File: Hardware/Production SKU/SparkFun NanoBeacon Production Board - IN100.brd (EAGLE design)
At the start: 25.4 x 25.4 mm, 63 parts, among them J3 Vertical Qwiic Connector, U1 IN100, Y1 CRYSTAL-26MHZSMD-3.2X2.5

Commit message: v11 updates
Bump version number
Update board name in silk
Change "VBATT" silk to "Battery"
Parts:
- removed U$10: (no value), output:BEACON_#_IN1000
- removed U$27: (no value), output:VBATT_OR_VCC_ONLY##0
- added U$29: (no value), output:NANOBEACON0
- added U$31: (no value), output:IN1000
- U$1: device output:BLUETOOTH0 -> output:NANOBEACON0
- U$5: device output:BEACON_#_IN1000 -> output:IN1000
- U$9: device output:BLUETOOTH0 -> output:BATTERY_OR_VCC_ONLY##0
- moved U$9 18.4 mm to (12.7, 0.89), flipped to the top
- moved U$5 2.92 mm to (12.7, 17.5), flipped to the bottom
- moved U$1 2.67 mm to (12.7, 19.2), flipped to the bottom
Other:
- board text added: "v11"
- board text removed: "v10"
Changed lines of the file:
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@@
 <drawing>
 <settings>
-<setting alwaysvectorfont="no"/>
+<setting alwaysvectorfont="yes"/>
 <setting verticaltext="up"/>
 </settings>
@@
 <vertex x="21.865" y="18.33"/>
 </polygon>
-<text x="12.7" y="0.889" size="1.27" layer="16" font="vector" ratio="15" rot="MR0" align="center">v10</text>
+<text x="12.7" y="0.889" size="1.27" layer="16" font="vector" ratio="15" rot="MR0" align="center">v11</text>
 <polygon width="0.1016" layer="22">
 <vertex x="19.05" y="8.89"/>
@@
 <attribute name="VALUE" x="16.48366875" y="15.224" size="0.6096" layer="27" rot="R270"/>
 </element>
-<element name="U$1" library="output" package="BLUETOOTH0" value="" x="12.7" y="21.844" smashed="yes"/>
 <element name="U$4" library="SparkFun-Aesthetics" package="SFE_LOGO_NAME_.1" value="" x="12.7" y="23.749" smashed="yes"/>
-<element name="U$5" library="output" package="BEACON_#_IN1000" value="" x="12.7" y="20.447" smashed="yes"/>
 <element name="U$2" library="output" package="#_7#0" value="" x="1.397" y="19.05" smashed="yes"/>
 <element name="U$3" library="output" package="#_6#0" value="" x="1.397" y="16.51" smashed="yes"/>
@@
 <element name="LOGO1" library="SparkFun-Aesthetics" package="OSHW-LOGO-S" value="OSHW-LOGOS" x="12.7" y="11.43" smashed="yes" rot="MR0"/>
 <element name="LOGO2" library="SparkFun-Aesthetics" package="SFE_LOGO_NAME_FLAME_.1" value="SFE_LOGO_NAME_FLAME.1_INCH" x="12.7" y="21.59" smashed="yes" rot="MR0"/>
-<element name="U$9" library="output" package="BLUETOOTH0" value="" x="12.7" y="19.304" smashed="yes" rot="MR0"/>
-<element name="U$10" library="output" package="BEACON_#_IN1000" value="" x="12.7" y="17.907" smashed="yes" rot="MR0"/>
 <element name="U$13" library="output" package="#IO7_#0" value="" x="1.27" y="19.05" smashed="yes" rot="MR0"/>
 <element name="U$14" library="output" package="#IO6_#0" value="" x="1.27" y="16.51" smashed="yes" rot="MR0"/>
@@
 <element name="U$26" library="output" package="PWR0" value="" x="5.08" y="9.271" smashed="yes"/>
 <element name="U$12" library="output" package="#NOTES#0" value="" x="16.129" y="8.89" smashed="yes" rot="MR0"/>
-<element name="U$27" library="output" package="VBATT_OR_VCC_ONLY##0" value="" x="12.7" y="0.889" smashed="yes"/>
 <element name="RST" library="SparkFun-Switches" package="TACTILE_SWITCH_SMD_4.6X2.8MM" value="DNP" x="6.35" y="14.732" smashed="yes">
 <attribute name="NAME" x="6.35" y="16.256" size="0.6096" layer="25" font="vector" ratio="20" align="bottom-center"/>
@@
 <element name="U$30" library="output" package="PRO0" value="" x="21.59" y="24.003" smashed="yes"/>
 <element name="TP3" library="SparkFun-Connectors" package="PAD.03X.03" value="TEST-POINT3" x="6.35" y="15.875" smashed="yes" rot="MR0"/>
+<element name="U$29" library="output" package="NANOBEACON0" value="" x="12.7" y="21.844" smashed="yes"/>
+<element name="U$31" library="output" package="IN1000" value="" x="12.7" y="20.32" smashed="yes"/>
+<element name="U$1" library="output" package="NANOBEACON0" value="" x="12.7" y="19.177" smashed="yes" rot="MR0"/>
+<element name="U$5" library="output" package="IN1000" value="" x="12.7" y="17.526" smashed="yes" rot="MR0"/>
+<element name="U$9" library="output" package="BATTERY_OR_VCC_ONLY##0" value="" x="12.7" y="0.889" smashed="yes"/>
 </elements>
 <signals>

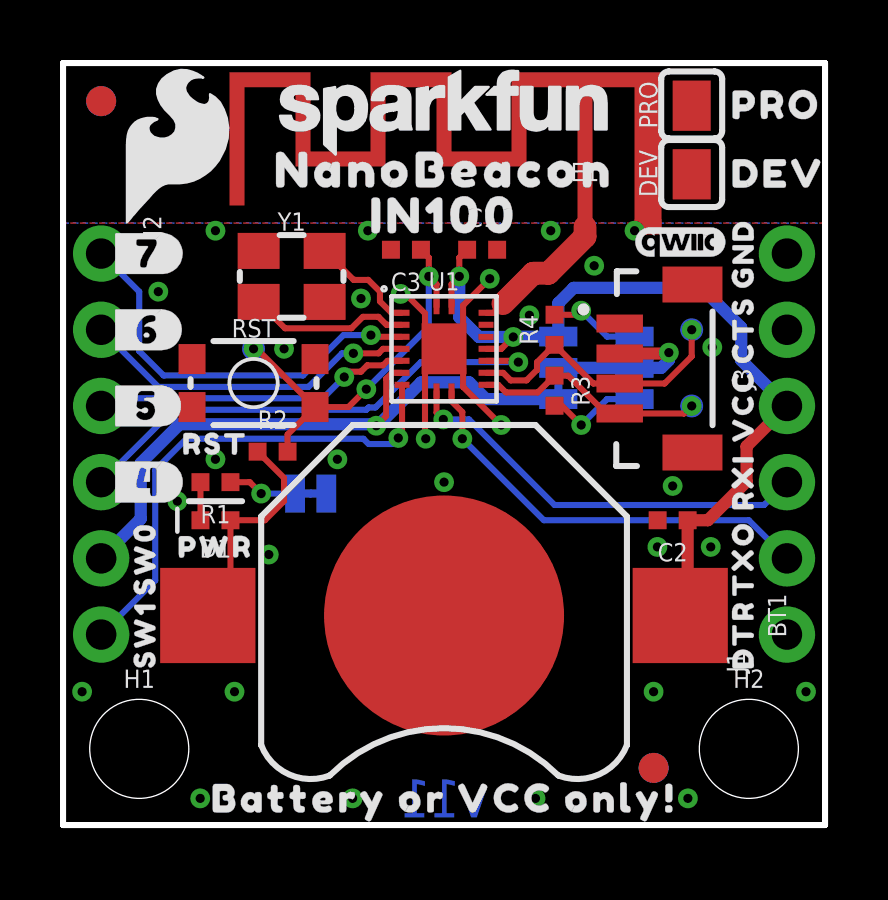
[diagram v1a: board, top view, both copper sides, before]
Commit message: Minor updates
Nudge bottom SFE silk logo away from edge
Increase size of Qwiic logo
Nudge vias along bottom edge
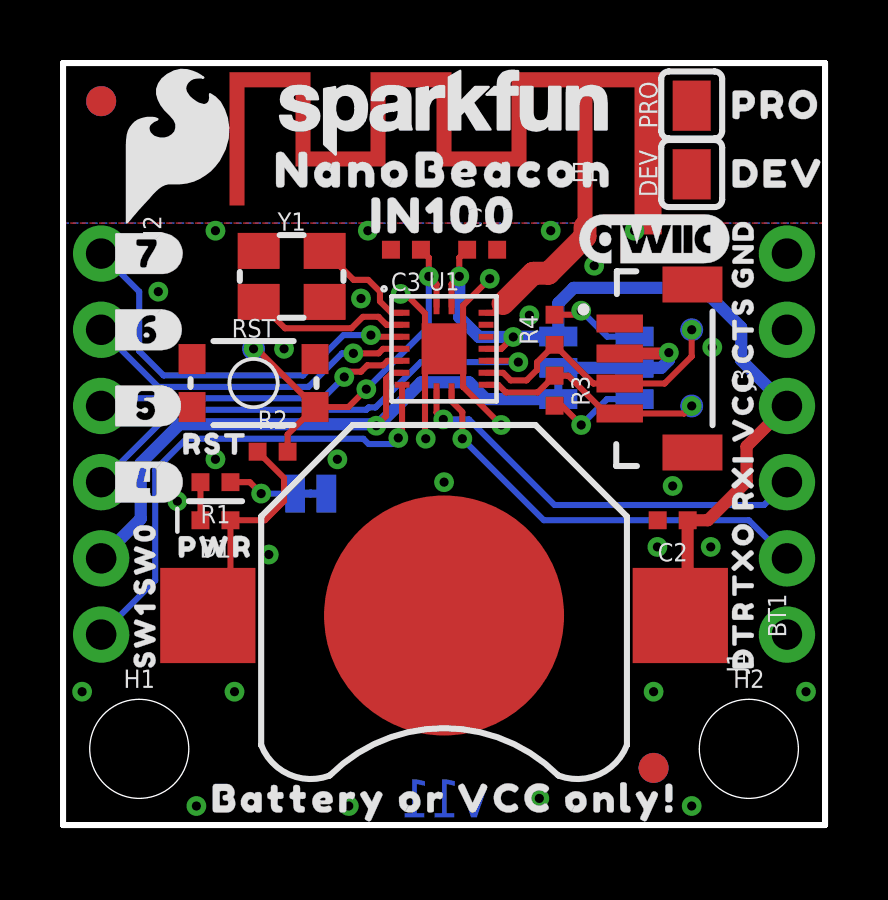
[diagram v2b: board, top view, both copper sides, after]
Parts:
- LOGO3: value QWIIC_LOGO_3MM -> QWIIC_LOGO_5MM; device SparkFun-Aesthetics:QWIIC_3MM -> SparkFun-Aesthetics:QWIIC_5MM
- moved LOGO3 0.90 mm to (19.7, 19.6)
- moved LOGO2 0.13 mm to (12.7, 21.5)
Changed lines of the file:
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@@
 <layer number="46" name="Milling" color="3" fill="1" visible="yes" active="yes"/>
 <layer number="47" name="Measures" color="7" fill="1" visible="yes" active="yes"/>
-<layer number="48" name="Document" color="7" fill="1" visible="no" active="yes"/>
+<layer number="48" name="Document" color="7" fill="1" visible="yes" active="yes"/>
 <layer number="49" name="Reference" color="7" fill="1" visible="no" active="yes"/>
 <layer number="50" name="dxf" color="7" fill="1" visible="no" active="no"/>
@@
 <element name="U$8" library="SparkFun-Aesthetics" package="SFE_LOGO_FLAME_.2" value="" x="3.81" y="22.606" smashed="yes"/>
 <element name="LOGO1" library="SparkFun-Aesthetics" package="OSHW-LOGO-S" value="OSHW-LOGOS" x="12.7" y="11.43" smashed="yes" rot="MR0"/>
-<element name="LOGO2" library="SparkFun-Aesthetics" package="SFE_LOGO_NAME_FLAME_.1" value="SFE_LOGO_NAME_FLAME.1_INCH" x="12.7" y="21.59" smashed="yes" rot="MR0"/>
+<element name="LOGO2" library="SparkFun-Aesthetics" package="SFE_LOGO_NAME_FLAME_.1" value="SFE_LOGO_NAME_FLAME.1_INCH" x="12.7" y="21.463" smashed="yes" rot="MR0"/>
 <element name="U$13" library="output" package="#IO7_#0" value="" x="1.27" y="19.05" smashed="yes" rot="MR0"/>
 <element name="U$14" library="output" package="#IO6_#0" value="" x="1.27" y="16.51" smashed="yes" rot="MR0"/>
@@
 </element>
 <element name="U$23" library="output" package="RST0" value="" x="5.08" y="12.7" smashed="yes"/>
-<element name="LOGO3" library="SparkFun-Aesthetics" package="QWIIC_3MM" value="QWIIC_LOGO_3MM" x="20.574" y="19.431" smashed="yes"/>
+<element name="LOGO3" library="SparkFun-Aesthetics" package="QWIIC_5MM" value="QWIIC_LOGO_5MM" x="19.685" y="19.558" smashed="yes"/>
 <element name="U$28" library="output" package="DEV0" value="" x="21.59" y="21.717" smashed="yes"/>
 <element name="PRO" library="SparkFun-Aesthetics" package="PRODUCT_IDENT_PASTE_SILK" value="PROD_ID_PASTE_SILK" x="20.955" y="24.003" smashed="yes" rot="R90">
@@
 <wire x1="14.605" y1="13.335" x2="13.335" y2="14.605" width="0.2032" layer="1"/>
 <via x="6.858" y="9.017" extent="1-16" drill="0.3048"/>
-<via x="4.572" y="0.889" extent="1-16" drill="0.3048"/>
-<via x="20.828" y="0.889" extent="1-16" drill="0.3048"/>
-<via x="15.748" y="0.889" extent="1-16" drill="0.3048"/>
-<via x="9.652" y="0.889" extent="1-16" drill="0.3048"/>
+<via x="4.445" y="0.635" extent="1-16" drill="0.3048"/>
+<via x="20.955" y="0.635" extent="1-16" drill="0.3048"/>
+<via x="15.875" y="0.889" extent="1-16" drill="0.3048"/>
+<via x="9.525" y="0.635" extent="1-16" drill="0.3048"/>
 <via x="20.32" y="11.303" extent="1-16" drill="0.3048"/>
 <via x="12.7" y="11.43" extent="1-16" drill="0.3048"/>
